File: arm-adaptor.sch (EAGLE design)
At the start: 3 parts, among them IC2 ATMEGA644-20PU

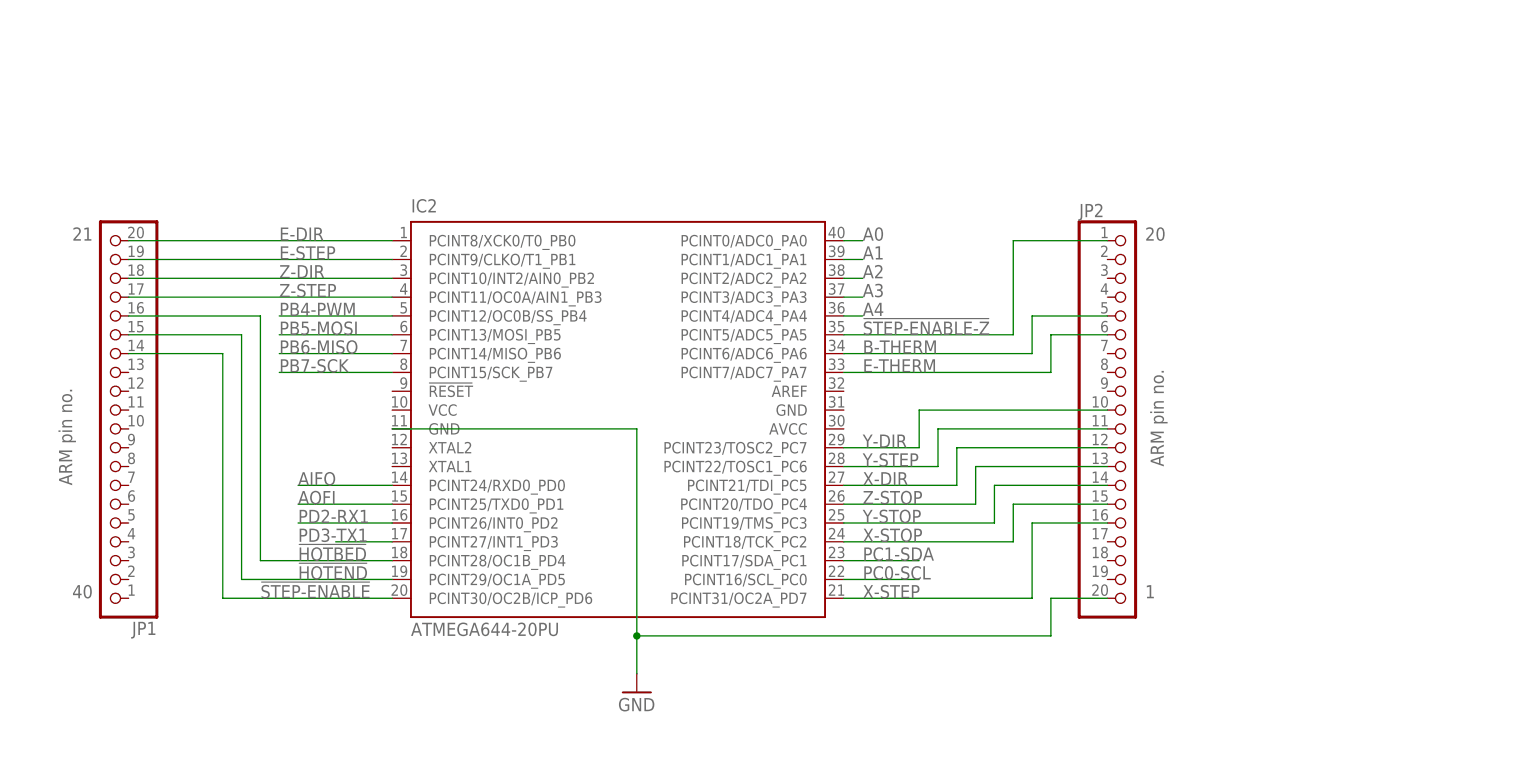
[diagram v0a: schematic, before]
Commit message: Added SD card and potential dividers on analogue inputs.
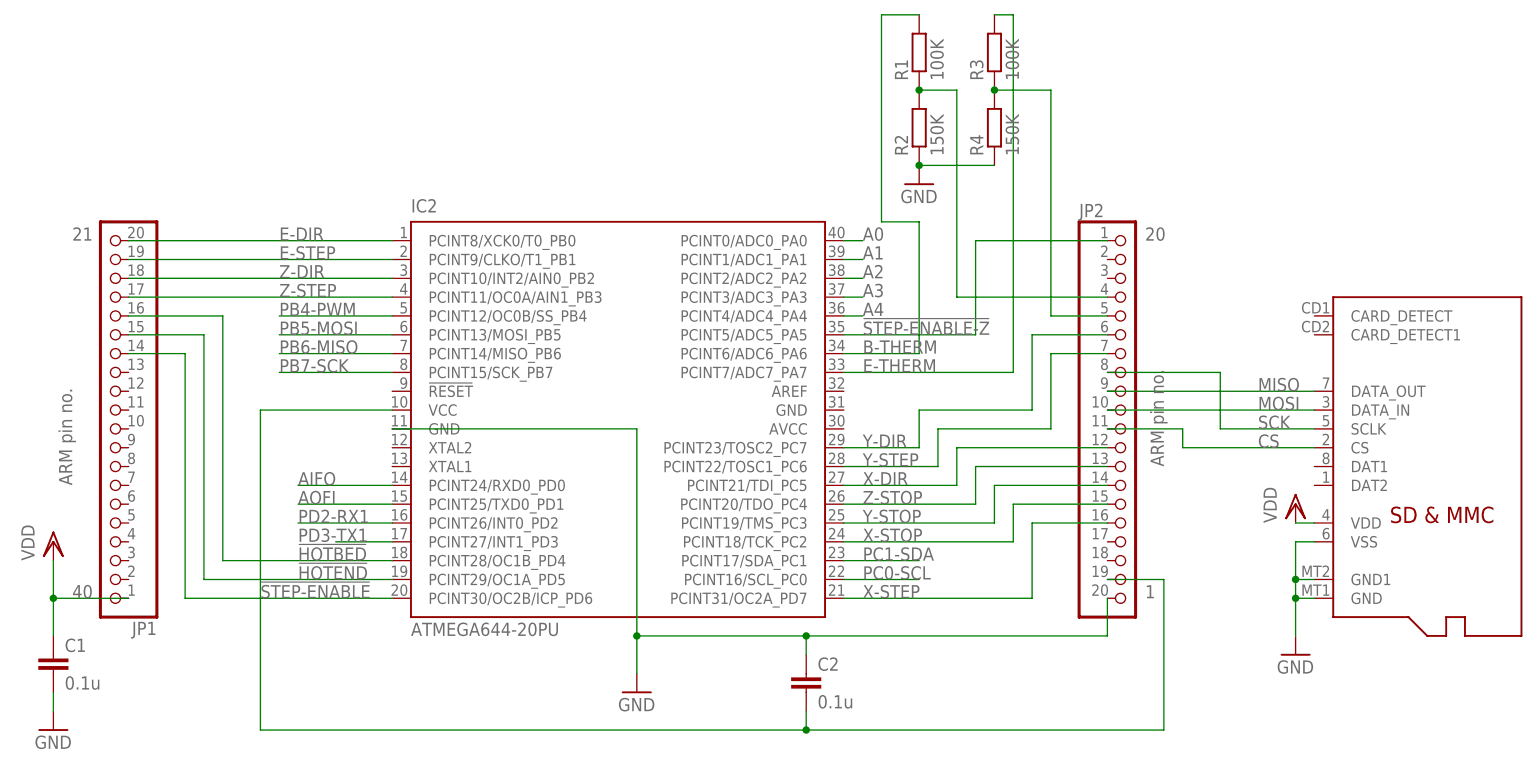
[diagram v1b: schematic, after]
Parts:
- added C1, C2: 0.1u, rcl:C-EU025-024X044
- added R1, R3: 100K, rcl:R-EU_0204/5
- added R2, R4: 150K, rcl:R-EU_0204/5
- added X1: MICROSD, adafruit:MICROSD
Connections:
- new net CS: JP2.11, X1.CS
- new net MISO: JP2.9, X1.DATA_OUT
- new net MOSI: JP2.10, X1.DATA_IN
- new net N$1: JP2.4, R1.1, R2.2
- new net N$2: JP2.5, R3.1, R4.2
- new net SCK: JP2.8, X1.SCLK
- new net VDD: C1.1, JP1.1, X1.VDD
- new net VIN: C2.2, IC2.VCC, JP2.19
- net B-THERM: now also R1.2; no longer JP2.5
- net E-THERM: now also R3.2; no longer JP2.6
- net GND: now also C1.2, C2.1, R2.1, R4.1, X1.GND, X1.GND1, X1.VSS
- net Y-DIR: now also JP2.6; no longer JP2.10
- net Y-STEP: now also JP2.7; no longer JP2.11
